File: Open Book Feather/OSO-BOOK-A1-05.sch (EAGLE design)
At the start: 127 parts, among them J1 SJ-43514-SMT, J2 10118193-0001LF, Q1 DMG341, Q2 IRLML0100, SW1 SPDT_SWITCH, U1 AP2112-3.3, U2 MCP73831T-2ACI/OT, U3 ATSAMD51J64-TQFP(10X10), U4 GD25Q16C (or GD25Q32C), U5 74AC165D, U6 GD25Q16C (or GD25Q32C), U7 MAX4468EKAT, X1 JSTPH, X2 2x5 0.05" SWD

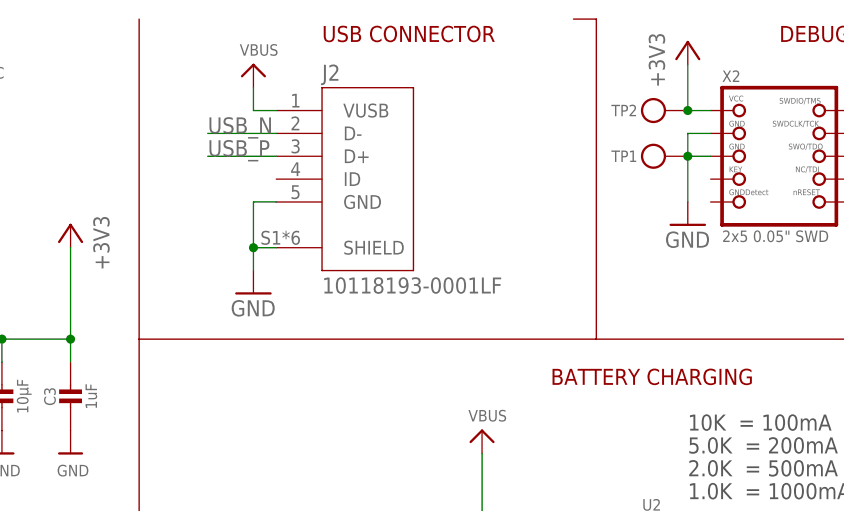
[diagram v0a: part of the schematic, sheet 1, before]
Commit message: connect shield to ground via RC (reduce headphone noise?)
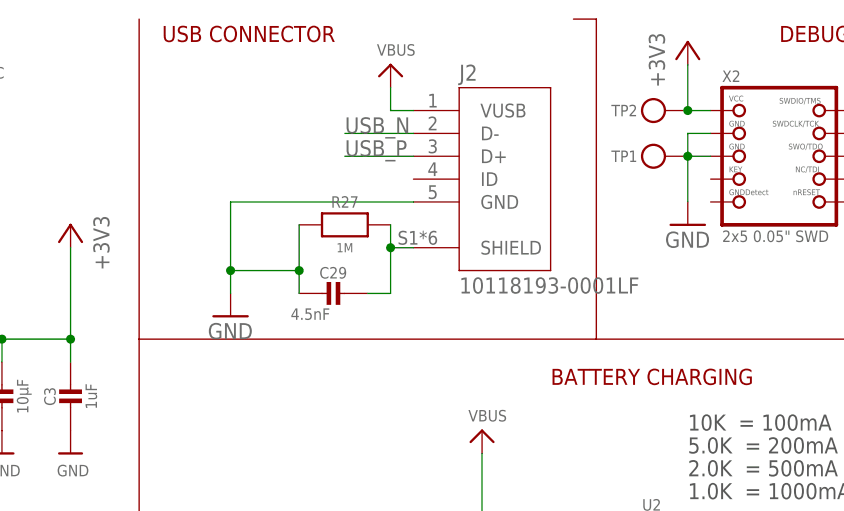
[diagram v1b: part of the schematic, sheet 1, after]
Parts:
- added C29: 4.5nF, microbuilder:CAP_CERAMIC0805-NOOUTLINE
- added R27: 1M, microbuilder:RESISTOR0805_NOOUTLINE
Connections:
- new net SHIELD: C29.1, J2.SHIELD, R27.1
- net GND: now also C29.2, R27.2; no longer J2.SHIELD
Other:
- moved on the sheet: J2
